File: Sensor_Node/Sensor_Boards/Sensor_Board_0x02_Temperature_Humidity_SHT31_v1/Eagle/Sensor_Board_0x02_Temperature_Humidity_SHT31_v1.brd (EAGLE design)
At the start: 55 x 35 mm, 16 parts, among them J1 M04_SMD_90, J4 ARDUINO_ISP, U2 ATMEGA328P_TQFP, Y1 8MHZ

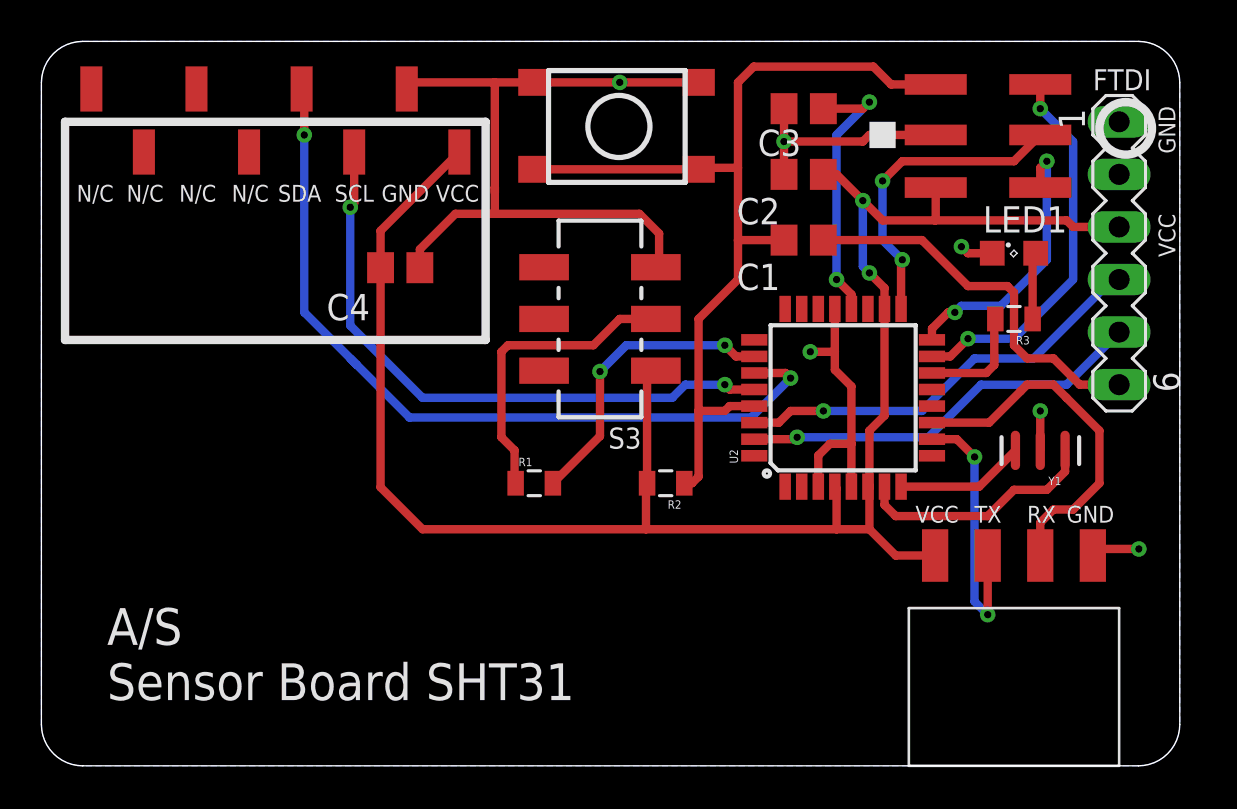
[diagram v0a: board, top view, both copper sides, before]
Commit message: Finished SHT31 and CO2-Board
- finished tidying SHT31
- added FTDI-connector to CO2-Sensorboard
- tidied CO2-Sensorboard
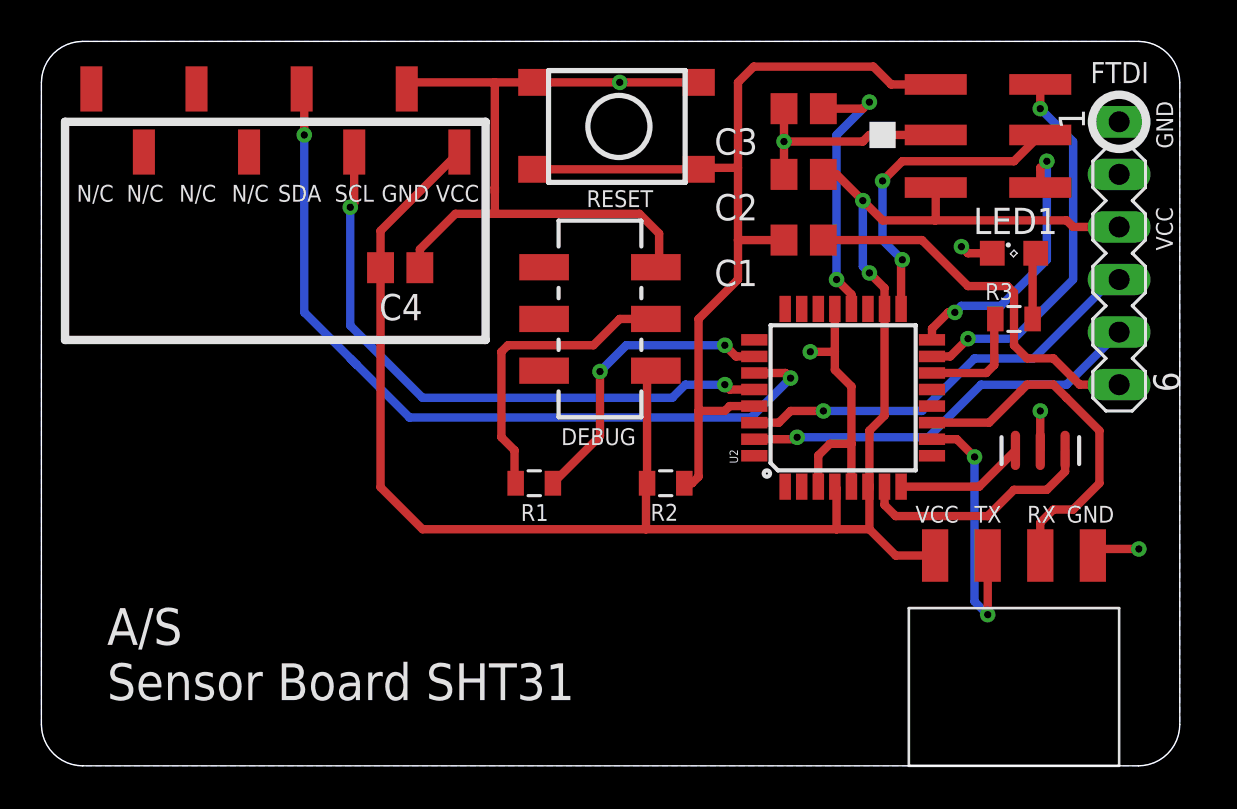
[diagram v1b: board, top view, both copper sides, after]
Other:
- board text added: "DEBUG"
- board text added: "RESET"
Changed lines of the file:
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@@
 <text x="3.175" y="3.175" size="1.778" layer="21">A/S
 Sensor Board SHT31</text>
-<circle x="52.3875" y="30.7975" radius="1.27" width="0.4064" layer="21"/>
+<circle x="52.07" y="31.115" radius="1.309084375" width="0.4064" layer="21"/>
 <text x="3.4925" y="28.067" size="0.8128" layer="21" rot="R180">N/C</text>
-<text x="53.975" y="26.67" size="0.8128" layer="21" rot="R270">VCC</text>
-<text x="50.8" y="32.639" size="1.016" layer="21">FTDI</text>
-<text x="53.975" y="31.877" size="0.8128" layer="21" rot="R270">GND</text>
+<text x="53.853340625" y="26.9864" size="0.8128" layer="21" rot="R270">VCC</text>
+<text x="50.68331875" y="32.9852" size="1.016" layer="21">FTDI</text>
+<text x="53.865509375" y="32.1203875" size="0.8128" layer="21" rot="R270">GND</text>
 <rectangle x1="40.005" y1="29.845" x2="41.275" y2="31.115" layer="21"/>
 <dimension x1="43.18" y1="10.16" x2="0" y2="10.16" x3="21.59" y3="-5.3975" textsize="1.778" layer="47"/>
+<text x="29.553896875" y="27.8079125" size="0.8128" layer="21" rot="R180">RESET</text>
+<text x="28.718196875" y="16.308665625" size="0.8128" layer="21" rot="R180">DEBUG</text>
 </plain>
 <attributes>
@@
 <elements>
 <element name="C3" library="eagle-ltspice" package="C0805" value="100n" x="36.83" y="31.75" smashed="yes" rot="R180">
-<attribute name="NAME" x="36.703" y="30.734" size="1.27" layer="25" rot="R180"/>
+<attribute name="NAME" x="34.6075" y="30.7975" size="1.27" layer="25" rot="R180"/>
 <attribute name="SPICEMODEL" value="NONE" x="36.83" y="31.75" size="1.778" layer="27" rot="R180" display="off"/>
 <attribute name="SPICEPREFIX" value="C" x="36.83" y="31.75" size="1.778" layer="27" rot="R180" display="off"/>
 </element>
 <element name="C2" library="eagle-ltspice" package="C0805" value="100n" x="36.83" y="28.575" smashed="yes" rot="R180">
-<attribute name="NAME" x="35.687" y="27.432" size="1.27" layer="25" rot="R180"/>
+<attribute name="NAME" x="34.6075" y="27.6225" size="1.27" layer="25" rot="R180"/>
 <attribute name="SPICEMODEL" value="NONE" x="36.83" y="28.575" size="1.778" layer="27" rot="R180" display="off"/>
 <attribute name="SPICEPREFIX" value="C" x="36.83" y="28.575" size="1.778" layer="27" rot="R180" display="off"/>
 </element>
 <element name="J4" library="marc_library" package="M-2X3" value="ARDUINO_ISP" x="48.26" y="27.94" rot="R90"/>
-<element name="LED1" library="led" package="SML0805" value="Red" x="46.99" y="24.765"/>
-<element name="R2" library="SparkFun-Passives" package="0805" value="10k" x="30.1625" y="13.6525" rot="R180"/>
-<element name="R1" library="SparkFun-Passives" package="0805" value="10k" x="23.8125" y="13.6525"/>
-<element name="R3" library="SparkFun-Passives" package="0805" value="330" x="46.99" y="21.59" rot="R180"/>
+<element name="LED1" library="led" package="SML0805" value="Red" x="46.99" y="24.765" smashed="yes">
+<attribute name="NAME" x="45.0277" y="25.691984375" size="1.27" layer="25"/>
+</element>
+<element name="R2" library="SparkFun-Passives" package="0805" value="10k" x="30.1625" y="13.6525" smashed="yes" rot="R180">
+<attribute name="NAME" x="30.764603125" y="12.652421875" size="0.8128" layer="25" rot="R180"/>
+</element>
+<element name="R1" library="SparkFun-Passives" package="0805" value="10k" x="23.8125" y="13.6525" smashed="yes">
+<attribute name="NAME" x="23.1629" y="11.83135" size="0.8128" layer="25"/>
+</element>
+<element name="R3" library="SparkFun-Passives" package="0805" value="330" x="46.99" y="21.59" smashed="yes" rot="R180">
+<attribute name="NAME" x="46.934403125" y="23.32004375" size="0.8128" layer="25" rot="R180"/>
+</element>
 <element name="S1" library="marc_library" package="M-PUSHBUTTON-SMD" value="Reset" x="23.8125" y="33.02"/>
 <element name="U2" library="marc_library" package="TQFP32-08" value="ATMEGA328P_TQFP" x="38.735" y="17.78" rot="R90">
 <attribute name="PROD_ID" value="IC-09069" x="38.735" y="17.78" size="1.778" layer="27" rot="R90" display="off"/>
 </element>
-<element name="Y1" library="marc_library" package="RESONATOR-SMD" value="8MHZ" x="48.26" y="15.24" rot="R180">
+<element name="Y1" library="marc_library" package="RESONATOR-SMD" value="8MHZ" x="48.26" y="15.24" smashed="yes" rot="R180">
 <attribute name="PROD_ID" value="XTAL-08895" x="48.26" y="15.24" size="1.778" layer="27" rot="R180" display="off"/>
 </element>
 <element name="C4" library="eagle-ltspice" package="C0805" value="100n" x="17.3355" y="24.0665" smashed="yes">
-<attribute name="NAME" x="13.7795" y="21.5265" size="1.27" layer="25"/>
+<attribute name="NAME" x="16.3195" y="21.5265" size="1.27" layer="25"/>
 <attribute name="SPICEMODEL" value="NONE" x="17.3355" y="24.0665" size="1.778" layer="27" display="off"/>
 <attribute name="SPICEPREFIX" value="C" x="17.3355" y="24.0665" size="1.778" layer="27" display="off"/>
 </element>
-<element name="S3" library="myownthings" package="JS202011SCQN" value="JS202011SCQN" x="26.9875" y="21.59" rot="R90"/>
+<element name="S3" library="myownthings" package="JS202011SCQN" value="JS202011SCQN" x="26.9875" y="21.59" smashed="yes" rot="R90"/>
 <element name="J1" library="myownthings" package="M04_SMD_90" value="M04_SMD_90" x="43.18" y="10.16"/>
 <element name="SV1" library="con-lstb" package="MA06-1" value="" x="52.07" y="24.765" smashed="yes" rot="R270">
@@
 </element>
 <element name="C1" library="eagle-ltspice" package="C0805" value="100n" x="36.83" y="25.4" smashed="yes" rot="R180">
-<attribute name="NAME" x="35.687" y="24.257" size="1.27" layer="25" rot="R180"/>
+<attribute name="NAME" x="34.6075" y="24.4475" size="1.27" layer="25" rot="R180"/>
 <attribute name="SPICEMODEL" value="NONE" x="36.83" y="25.4" size="1.778" layer="27" rot="R180" display="off"/>
 <attribute name="SPICEPREFIX" value="C" x="36.83" y="25.4" size="1.778" layer="27" rot="R180" display="off"/>

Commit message: Updated Prototyping Board & DS18B20 Board
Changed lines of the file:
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@@
 <?xml version="1.0" encoding="utf-8"?>
 <!DOCTYPE eagle SYSTEM "eagle.dtd">
-<eagle version="8.4.2">
+<eagle version="8.4.3">
 <drawing>
 <settings>
@@
 <wire x1="35.8775" y1="28.5775" x2="35.88" y2="28.575" width="0.4064" layer="1"/>
 <wire x1="35.8775" y1="30.1625" x2="39.6875" y2="30.1625" width="0.4064" layer="1"/>
-<wire x1="21.9075" y1="27.6885" x2="21.9075" y2="27.94" width="0.4064" layer="1"/>
-<wire x1="21.9075" y1="27.94" x2="21.9075" y2="33.02" width="0.4064" layer="1"/>
+<wire x1="21.9075" y1="26.67" x2="21.9075" y2="33.02" width="0.4064" layer="1"/>
 <wire x1="29.845" y1="25.7175" x2="28.8925" y2="26.67" width="0.4064" layer="1"/>
 <wire x1="29.845" y1="25.7175" x2="29.845" y2="24.2475" width="0.4064" layer="1"/>
@@
 <wire x1="21.9075" y1="26.67" x2="28.8925" y2="26.67" width="0.4064" layer="1"/>
 <wire x1="21.9075" y1="26.67" x2="20.0025" y2="26.67" width="0.4064" layer="1"/>
-<wire x1="21.9075" y1="27.94" x2="21.9075" y2="26.67" width="0.4064" layer="1"/>
 </signal>
 <signal name="VCC" class="1">
